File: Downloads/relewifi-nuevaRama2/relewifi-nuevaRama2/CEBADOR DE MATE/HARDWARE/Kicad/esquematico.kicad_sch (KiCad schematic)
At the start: 50 parts, among them J1 Screw_Terminal_01x02, J10 LCD I2C, J12 Screw_Terminal_01x02, J13 Screw_Terminal_01x02, J14 Screw_Terminal_01x02, J15 Screw_Terminal_01x02, J2 Screw_Terminal_01x02, J3 Screw_Terminal_01x02, J4 Screw_Terminal_01x02, J5 Screw_Terminal_01x02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

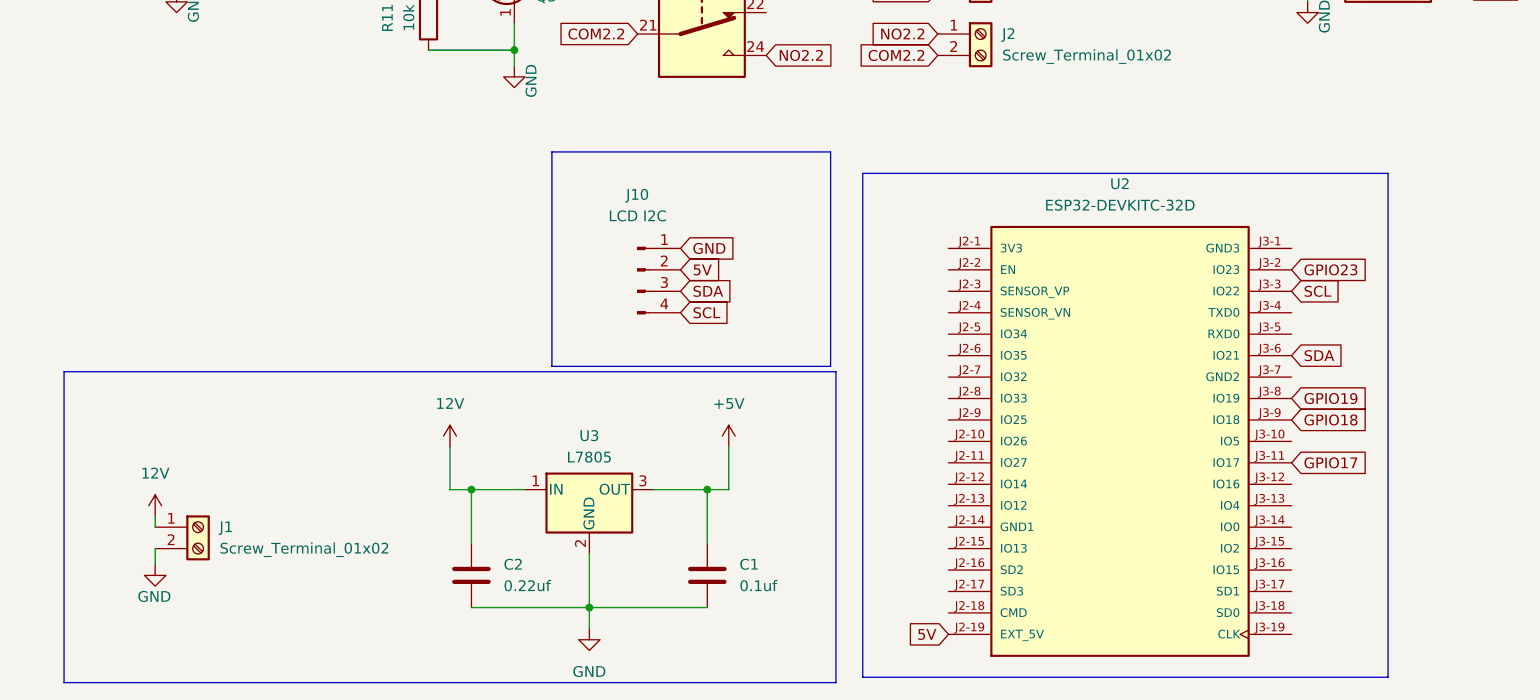
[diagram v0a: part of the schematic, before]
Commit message: termine el pcb y agregue una pinera para sensores,y agrande los pads y vias
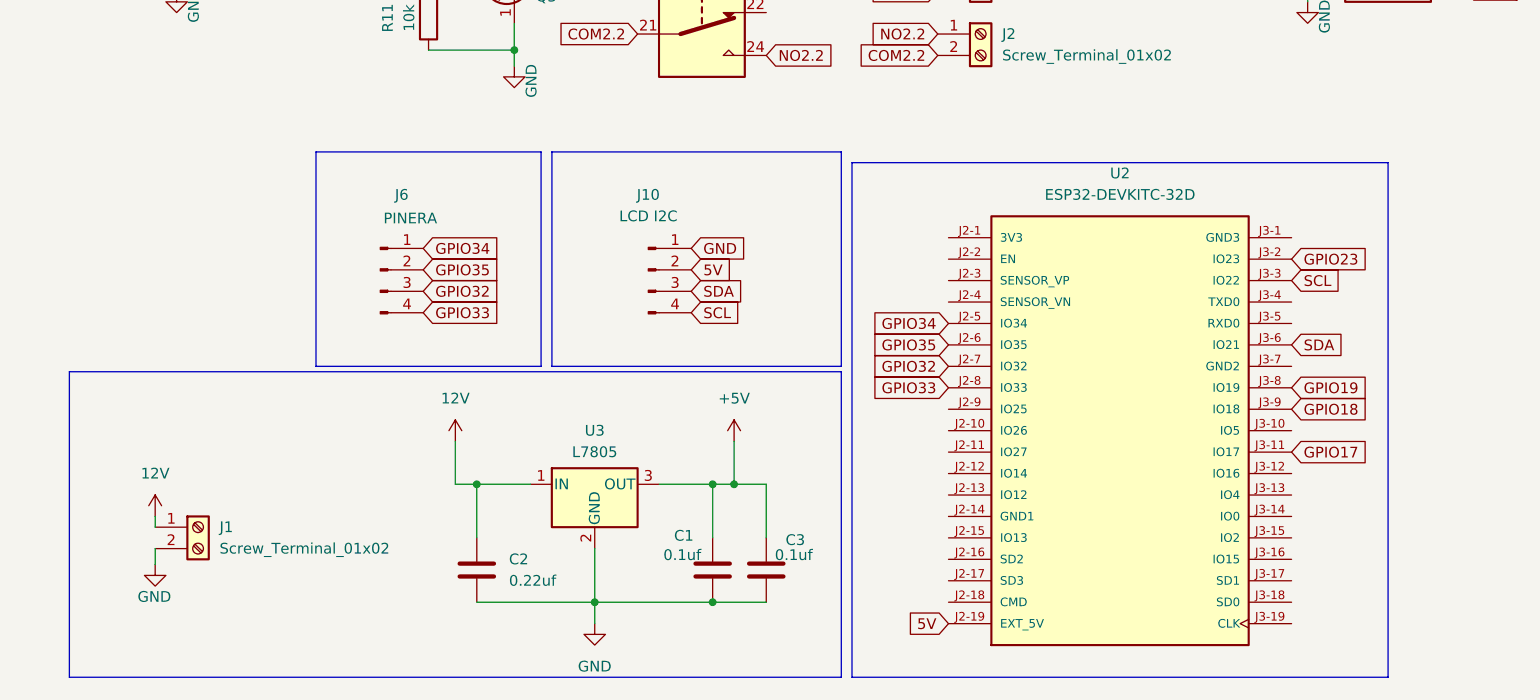
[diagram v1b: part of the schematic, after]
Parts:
- added C3: 0.1uf, Capacitor_SMD:C_0805_2012Metric_Pad1.18x1.45mm_HandSolder, symbol Device:C
- added J6: PINERA, Connector_PinHeader_2.54mm:PinHeader_1x04_P2.54mm_Vertical, symbol Connector:Conn_01x04_Pin
- U3: footprint Package_TO_SOT_SMD:TO-252-2 -> Package_TO_SOT_SMD:TO-263-3_TabPin2
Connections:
- net +5V: now also C3.1
- net GND: now also C3.2
- net GPIO34: now reaches U2.J2-5 (IO34)
- net GPIO34: now also J6.1 (Pin_1)
- net GPIO35: now reaches U2.J2-6 (IO35)
- net GPIO35: now also J6.2 (Pin_2)
- net GPIO32: now reaches U2.J2-7 (IO32)
- net GPIO32: now also J6.3 (Pin_3)
- net GPIO33: now reaches U2.J2-8 (IO33)
- net GPIO33: now also J6.4 (Pin_4)
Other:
- moved on the sheet: C1, C2, J10, U2, U3
